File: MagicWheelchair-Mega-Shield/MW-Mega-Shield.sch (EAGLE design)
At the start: 20 parts

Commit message: Update PCB, add PNG version
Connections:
- net TOUCH_DISABLE: now also B1.12; no longer B1.5
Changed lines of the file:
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@@
 </segment>
 <segment>
-<pinref part="B1" gate="G$1" pin="5"/>
-<wire x1="48.26" y1="43.18" x2="43.18" y2="43.18" width="0.1524" layer="91"/>
-<wire x1="43.18" y1="43.18" x2="43.18" y2="48.26" width="0.1524" layer="91"/>
-<wire x1="43.18" y1="48.26" x2="35.56" y2="48.26" width="0.1524" layer="91"/>
-<label x="15.24" y="48.26" size="1.778" layer="95"/>
+<pinref part="B1" gate="G$1" pin="12"/>
+<wire x1="48.26" y1="25.4" x2="15.24" y2="25.4" width="0.1524" layer="91"/>
+<label x="-5.08" y="25.4" size="1.778" layer="95"/>
 </segment>
 </net>

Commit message: Update PCB, better PNGs
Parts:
- removed INPUT_1, INPUT_OPT: 736880-49, con-conrad:736880-49
- removed R3: 30kOhm, rcl:R-US_R0603
- removed TOUCH_DISABLE: (no value), jumper:JP1E
- added R4: 30kOhm, rcl:R-US_R0603
- added S1: (no value), SparkFun-Retired:SWITCH-SPDTSMD
- added X1, X2: TOBU3, con-hirschmann:TOBU3
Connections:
- removed net CS8: JP3.12
- new net CS2: JP3.6
- new net N$3: R4.1, S1.P
- net GND: now also S1.S, X1.2, X2.2; no longer R3.1
- net INPUT_1: now also X1.1; no longer INPUT_1.2
- net INPUT_OPT: now also JP3.12, X2.1; no longer INPUT_OPT.2, JP3.6
- net TOUCH_DISABLE: now also R4.2; no longer R3.2, TOUCH_DISABLE.2
- net VIN: now also S1.O; no longer TOUCH_DISABLE.1

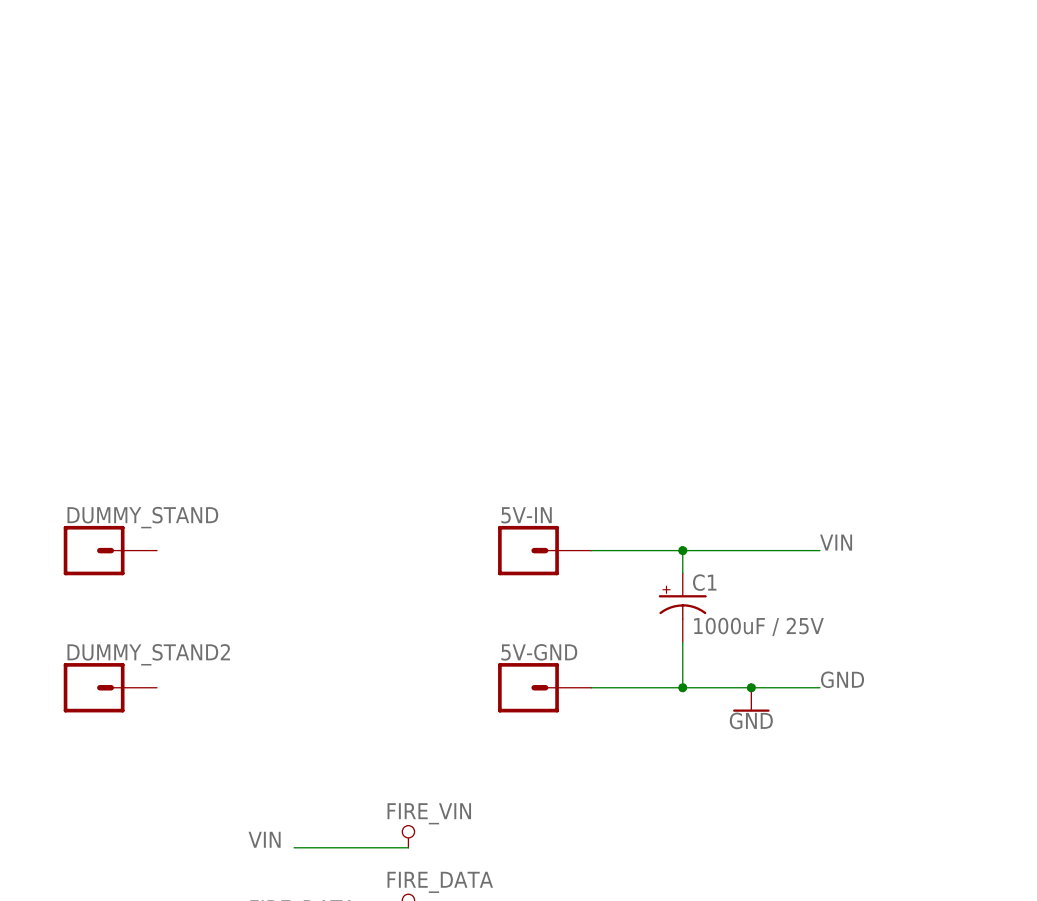
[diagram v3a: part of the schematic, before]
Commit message: Add master switch
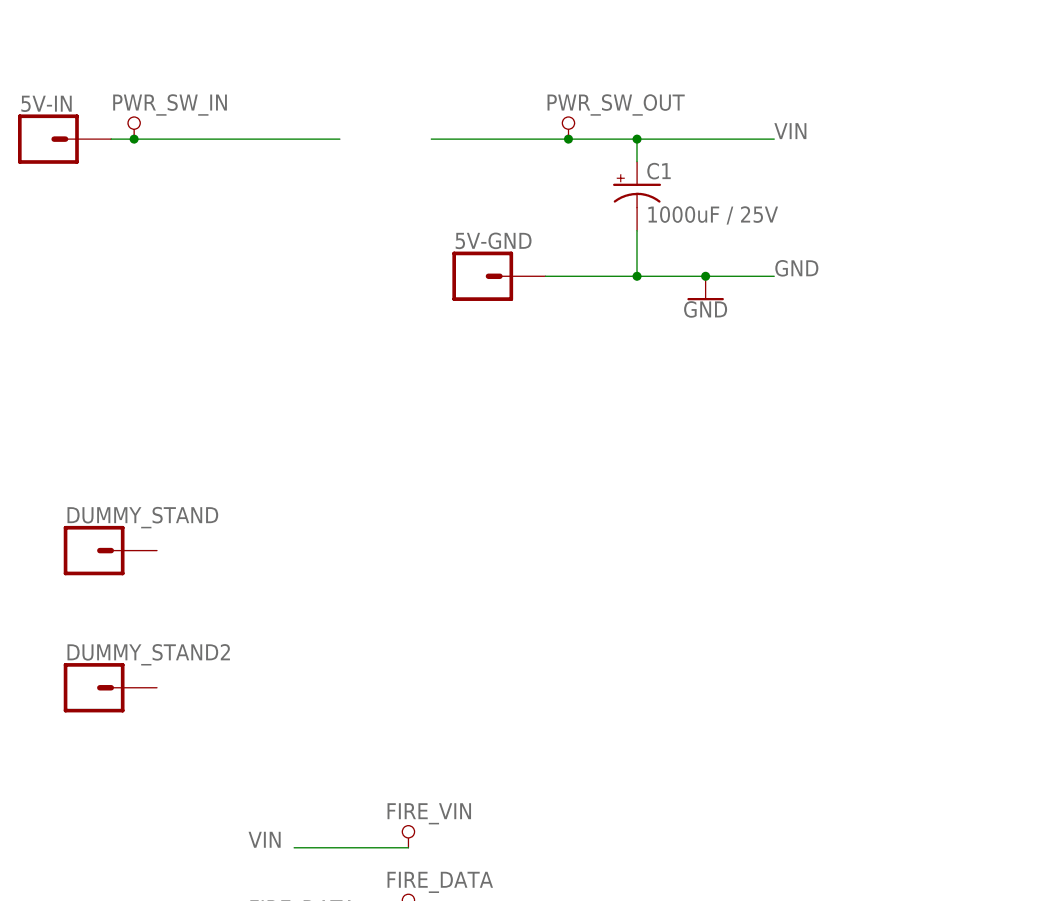
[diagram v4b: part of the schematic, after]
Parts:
- added PWR_SW_IN, PWR_SW_OUT: PAD_TERMINAL-1.02MM_SQUARE, dp_devices.v6:PAD_TERMINAL-1.02MM_SQUARE
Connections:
- new net N$6: 5V-IN.1, PWR_SW_IN.P
- net VIN: now also PWR_SW_OUT.P; no longer 5V-IN.1
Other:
- moved on the sheet: 5V-GND, 5V-IN, C1
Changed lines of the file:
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@@
 <part name="X1" library="con-hirschmann" library_urn="urn:adsk.eagle:library:153" deviceset="TOBU3" device="" package3d_urn="urn:adsk.eagle:package:7468/1"/>
 <part name="X2" library="con-hirschmann" library_urn="urn:adsk.eagle:library:153" deviceset="TOBU3" device="" package3d_urn="urn:adsk.eagle:package:7468/1"/>
+<part name="PWR_SW_IN" library="dp_devices.v6" deviceset="PAD_TERMINAL" device="-1.02MM_SQUARE"/>
+<part name="PWR_SW_OUT" library="dp_devices.v6" deviceset="PAD_TERMINAL" device="-1.02MM_SQUARE"/>
 </parts>
 <sheets>
@@
 <instance part="R1" gate="G$1" x="30.48" y="43.18"/>
 <instance part="R2" gate="G$1" x="30.48" y="35.56"/>
-<instance part="C1" gate="G$1" x="-12.7" y="96.52"/>
-<instance part="5V-IN" gate="G$1" x="-30.48" y="101.6"/>
-<instance part="5V-GND" gate="G$1" x="-30.48" y="86.36"/>
-<instance part="GND1" gate="1" x="-5.08" y="83.82"/>
+<instance part="C1" gate="G$1" x="-17.78" y="142.24"/>
+<instance part="5V-IN" gate="G$1" x="-83.82" y="147.32"/>
+<instance part="5V-GND" gate="G$1" x="-35.56" y="132.08"/>
+<instance part="GND1" gate="1" x="-10.16" y="129.54"/>
 <instance part="FIRE_VIN" gate="T" x="-43.18" y="71.12"/>
 <instance part="FIRE_DATA" gate="T" x="-43.18" y="63.5"/>
@@
 <instance part="X1" gate="B" x="101.6" y="149.86"/>
 <instance part="X2" gate="B" x="104.14" y="132.08"/>
+<instance part="PWR_SW_IN" gate="T" x="-73.66" y="149.86"/>
+<instance part="PWR_SW_OUT" gate="T" x="-25.4" y="149.86"/>
 </instances>
 <busses>
@@
 <pinref part="C1" gate="G$1" pin="-"/>
 <pinref part="5V-GND" gate="G$1" pin="1"/>
-<wire x1="-12.7" y1="91.44" x2="-12.7" y2="86.36" width="0.1524" layer="91"/>
-<wire x1="-12.7" y1="86.36" x2="-22.86" y2="86.36" width="0.1524" layer="91"/>
-<wire x1="-12.7" y1="86.36" x2="-5.08" y2="86.36" width="0.1524" layer="91"/>
-<label x="2.54" y="86.36" size="1.778" layer="95"/>
+<wire x1="-17.78" y1="137.16" x2="-17.78" y2="132.08" width="0.1524" layer="91"/>
+<wire x1="-17.78" y1="132.08" x2="-27.94" y2="132.08" width="0.1524" layer="91"/>
+<wire x1="-17.78" y1="132.08" x2="-10.16" y2="132.08" width="0.1524" layer="91"/>
+<label x="-2.54" y="132.08" size="1.778" layer="95"/>
 <pinref part="GND1" gate="1" pin="GND"/>
-<wire x1="-5.08" y1="86.36" x2="2.54" y2="86.36" width="0.1524" layer="91"/>
-<junction x="-5.08" y="86.36"/>
-<junction x="-12.7" y="86.36"/>
+<wire x1="-10.16" y1="132.08" x2="-2.54" y2="132.08" width="0.1524" layer="91"/>
+<junction x="-10.16" y="132.08"/>
+<junction x="-17.78" y="132.08"/>
 </segment>
 <segment>
@@
 </segment>
 <segment>
-<pinref part="5V-IN" gate="G$1" pin="1"/>
-<wire x1="-22.86" y1="101.6" x2="-12.7" y2="101.6" width="0.1524" layer="91"/>
 <pinref part="C1" gate="G$1" pin="+"/>
-<wire x1="-12.7" y1="101.6" x2="-12.7" y2="99.06" width="0.1524" layer="91"/>
-<wire x1="-12.7" y1="101.6" x2="2.54" y2="101.6" width="0.1524" layer="91"/>
-<label x="2.54" y="101.6" size="1.778" layer="95"/>
-<junction x="-12.7" y="101.6"/>
+<wire x1="-17.78" y1="147.32" x2="-17.78" y2="144.78" width="0.1524" layer="91"/>
+<wire x1="-17.78" y1="147.32" x2="-2.54" y2="147.32" width="0.1524" layer="91"/>
+<label x="-2.54" y="147.32" size="1.778" layer="95"/>
+<pinref part="PWR_SW_OUT" gate="T" pin="P"/>
+<wire x1="-40.64" y1="147.32" x2="-25.4" y2="147.32" width="0.1524" layer="91"/>
+<wire x1="-25.4" y1="147.32" x2="-17.78" y2="147.32" width="0.1524" layer="91"/>
+<junction x="-25.4" y="147.32"/>
+<junction x="-17.78" y="147.32"/>
 </segment>
 <segment>
@@
 </segment>
 </net>
+<net name="N$6" class="0">
+<segment>
+<pinref part="5V-IN" gate="G$1" pin="1"/>
+<pinref part="PWR_SW_IN" gate="T" pin="P"/>
+<wire x1="-76.2" y1="147.32" x2="-73.66" y2="147.32" width="0.1524" layer="91"/>
+<wire x1="-73.66" y1="147.32" x2="-50.8" y2="147.32" width="0.1524" layer="91"/>
+<junction x="-73.66" y="147.32"/>
+</segment>
+</net>

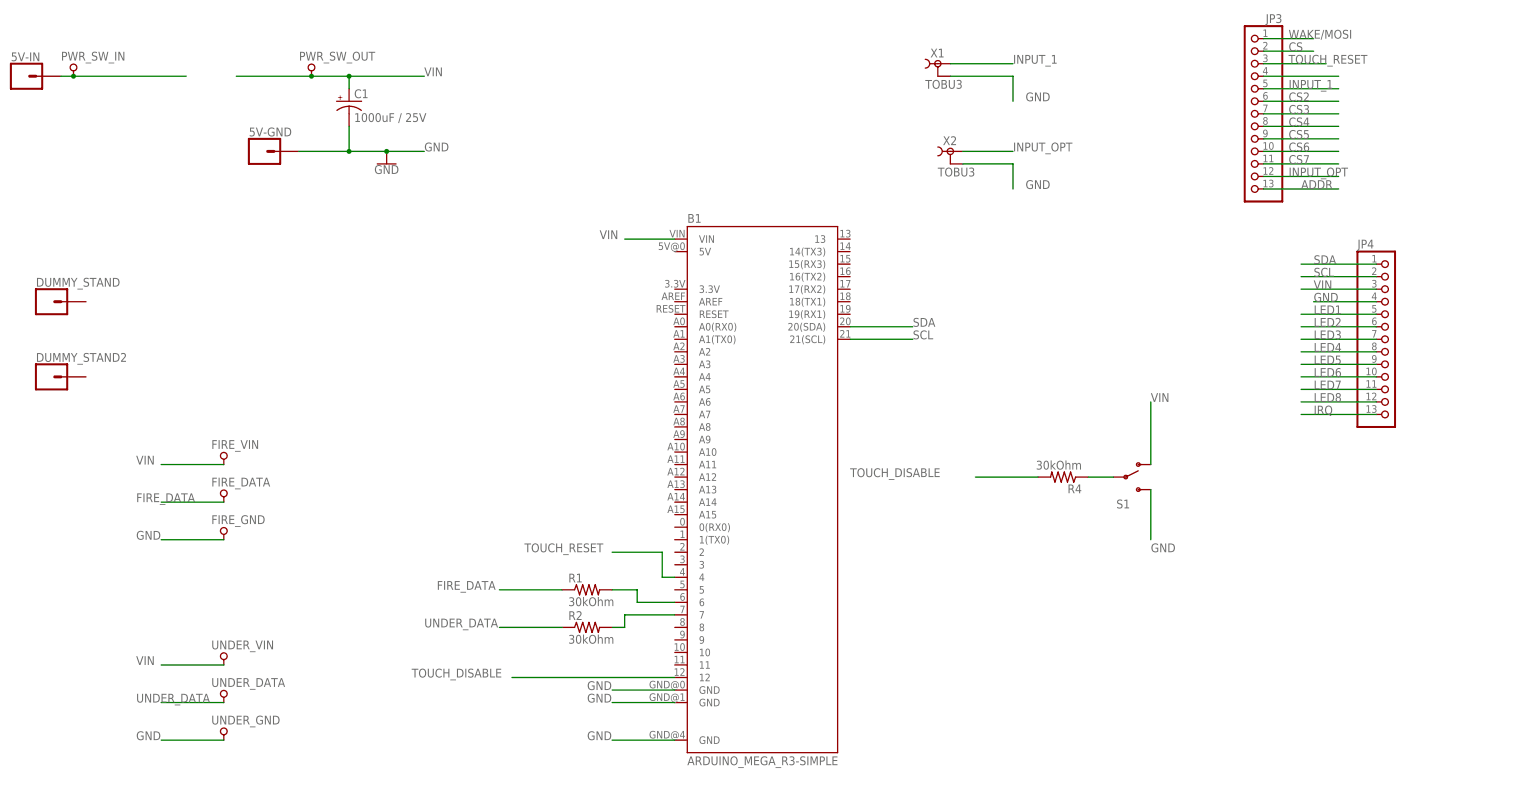
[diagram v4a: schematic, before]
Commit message: Merge shields into one
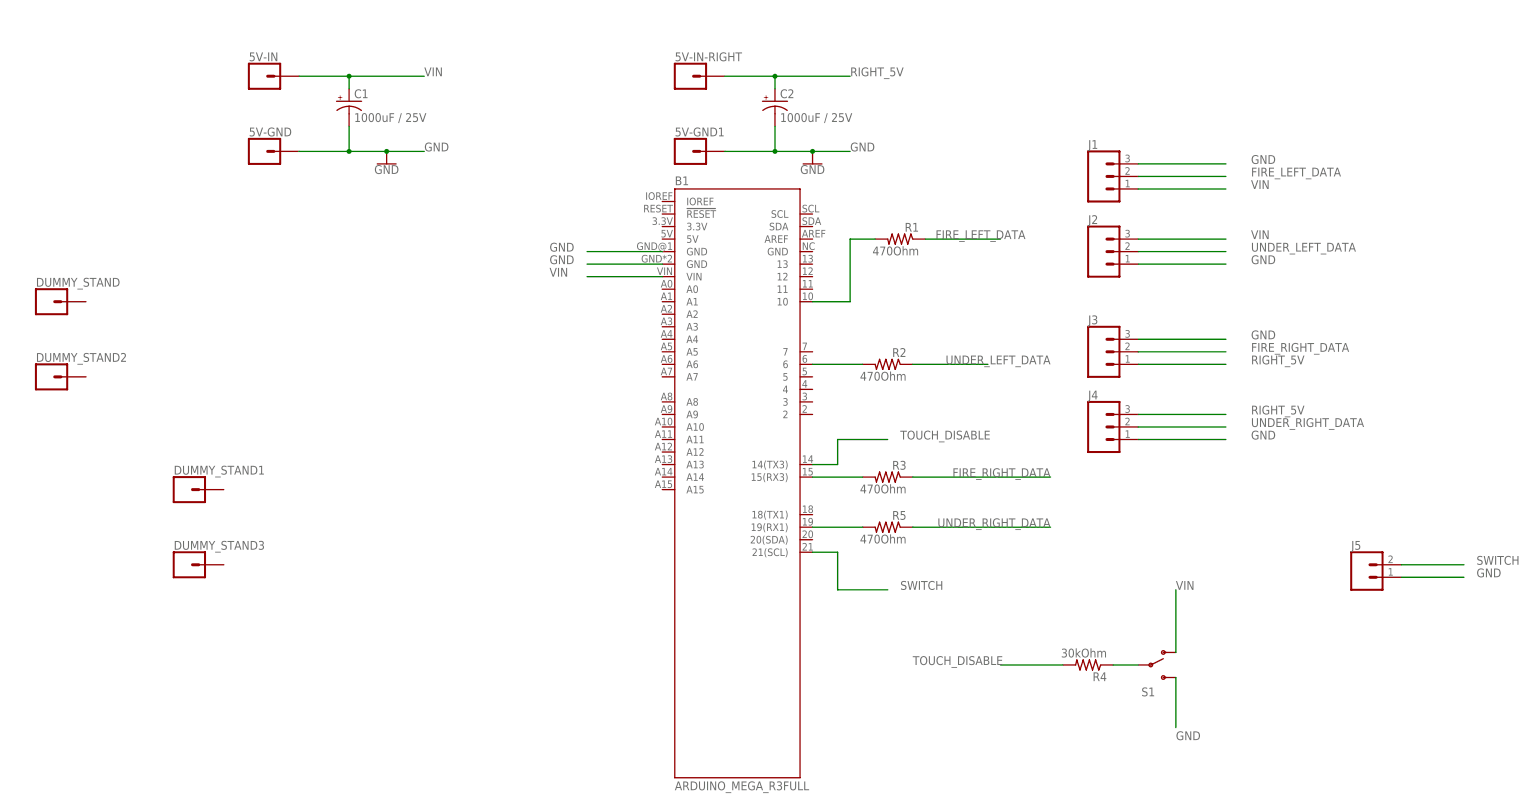
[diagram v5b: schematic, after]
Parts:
- removed FIRE_DATA, FIRE_GND, FIRE_VIN, PWR_SW_IN, PWR_SW_OUT, UNDER_DATA, UNDER_GND, UNDER_VIN: PAD_TERMINAL-1.02MM_SQUARE, dp_devices.v6:PAD_TERMINAL-1.02MM_SQUARE
- removed JP3, JP4: (no value), microbuilder:HEADER-1X13
- removed X1, X2: TOBU3, con-hirschmann:TOBU3
- added 5V-GND1, 5V-IN-RIGHT, DUMMY_STAND1, DUMMY_STAND3: (no value), SparkFun-Connectors:CONN_01
- added C2: 1000uF / 25V, rcl:CPOL-USE5-10.5
- added J1, J2, J3, J4: (no value), SparkFun-Connectors:CONN_03SCREW-NS
- added J5: (no value), SparkFun-Connectors:CONN_02
- added R3, R5: 470Ohm, rcl:R-US_R0603
- B1: value ARDUINO_MEGA_R3-SIMPLE -> ARDUINO_MEGA_R3FULL; device SparkFun-Boards:ARDUINO_MEGA_R3-SIMPLE -> SparkFun-Boards:ARDUINO_MEGA_R3FULL
- R1, R2: value 30kOhm -> 470Ohm
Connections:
- removed net ADDR: JP3.13
- removed net CS: JP3.2
- removed net CS2: JP3.6
- removed net CS3: JP3.7
- removed net CS4: JP3.8
- removed net CS5: JP3.9
- removed net CS6: JP3.10
- removed net CS7: JP3.11
- removed net FIRE_DATA: FIRE_DATA.P, R1.1
- removed net INPUT_1: JP3.5, X1.1
- removed net INPUT_OPT: JP3.12, X2.1
- removed net IRQ: JP4.13
- removed net LED1: JP4.5
- removed net LED2: JP4.6
- removed net LED3: JP4.7
- removed net LED4: JP4.8
- removed net LED5: JP4.9
- removed net LED6: JP4.10
- removed net LED7: JP4.11
- removed net LED8: JP4.12
- removed net N$6: 5V-IN.1, PWR_SW_IN.P
- removed net SCL: B1.21(SCL), JP4.2
- removed net SDA: B1.20(SDA), JP4.1
- removed net TOUCH_RESET: B1.4, JP3.3
- removed net UNDER_DATA: R2.1, UNDER_DATA.P
- removed net WAKE/MOSI: JP3.1
- new net FIRE_LEFT_DATA: J1.2, R1.1
- new net FIRE_RIGHT_DATA: J3.2, R3.1
- new net N$5: B1.19(RX1), R5.2
- new net RIGHT_5V: 5V-IN-RIGHT.1, C2.+, J3.1, J4.3
- new net SWITCH: B1.21(SCL), J5.2
- new net UNDER_LEFT_DATA: J2.2, R2.1
- new net UNDER_RIGHT_DATA: J4.2, R5.1
- net GND: now also 5V-GND1.1, B1.GND, B1.GND@2, C2.-, J1.3, J2.1, J3.3, J4.1, J5.1; no longer B1.GND@0, B1.GND@1, B1.GND@4, FIRE_GND.P, JP4.4, UNDER_GND.P, X1.2, X2.2
- net N$1: now also B1.10; no longer B1.6
- net N$2: now also B1.6; no longer B1.7
- net N$4: now also B1.15(RX3), R3.2; no longer JP3.4
- net TOUCH_DISABLE: now also B1.14(TX3); no longer B1.12
- net VIN: now also 5V-IN.1, J1.1, J2.3; no longer FIRE_VIN.P, JP4.3, PWR_SW_OUT.P, UNDER_VIN.P
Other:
- moved on the sheet: 5V-IN, R1, R2, R4, S1
